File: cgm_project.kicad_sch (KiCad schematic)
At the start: 0 parts

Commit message: feat: complete power management block with tp4056 and ap2112k
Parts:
- added C1, C2, C3: 10uF, symbol Device:C_Small
- added D1: GREEN LED, symbol Device:LED
- added D2: RED LED, symbol Device:LED
- added J1: JST BATT CONNECTOR, symbol Connector_Generic:Conn_01x02
- added R1: 2k, symbol Device:R_Small
- added R2: 1k, symbol Device:R_Small
- added SW1: SW_SPDT, symbol Switch:SW_SPDT
- added U1: TP4056-42-ESOP8, Package_SO:SOIC-8-1EP_3.9x4.9mm_P1.27mm_EP2.41x3.3mm_ThermalVias, symbol Battery_Management:TP4056-42-ESOP8
- added U2: AP2112K-3.3, Package_TO_SOT_SMD:SOT-23-5, symbol Regulator_Linear:AP2112K-3.3
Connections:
- new net: D1.1 (K), U1.6 (~{STDBY})
- new net: D1.2 (A), D2.2 (A), R1.2
- new net: R2.1, U1.2 (PROG)
- new net: SW1.2 (B), U2.1 (VIN), U2.3 (EN)
- new net: D2.1 (K), U1.7 (~{CHRG})
- new net +3V3: C3.1, U2.5 (VOUT)
- new net GND: C1.1, C2.2, C3.2, J1.2 (Pin_2), R2.2, U1.1 (TEMP), U1.3 (GND), U2.2 (GND)
- new net VBAT: C2.1, J1.1 (Pin_1), SW1.1 (A), U1.5 (BAT)
- new net VBUS_5V: C1.2, R1.1, U1.4 (V_{CC}), U1.8 (CE)
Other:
- note added: "POWER MANAGEMENT"

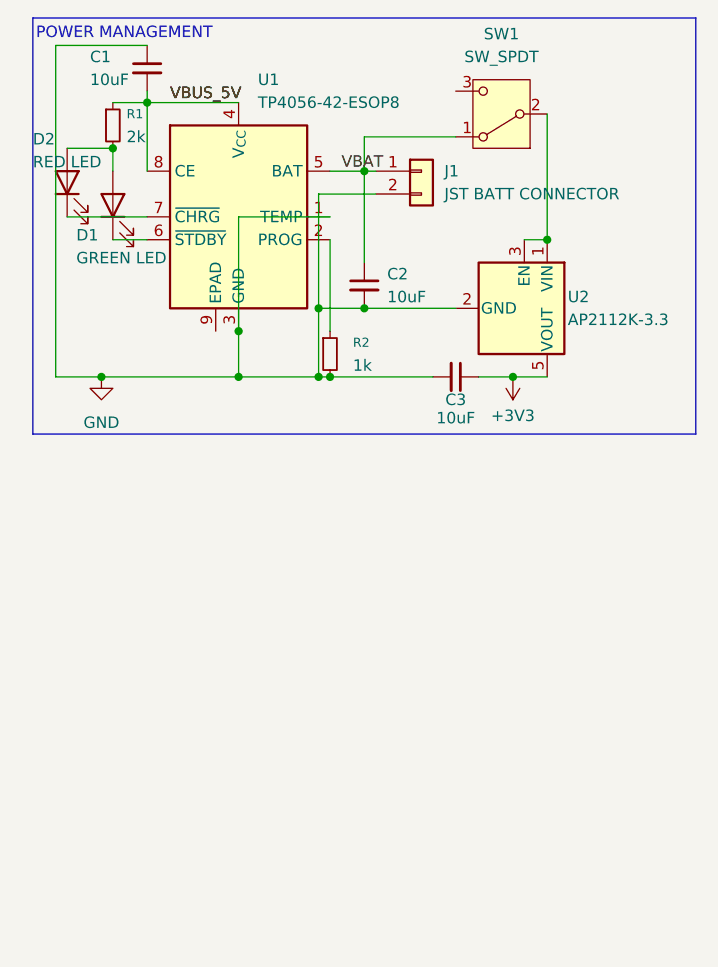
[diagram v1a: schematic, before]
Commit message: feat: implement fused native USB-C receptacle block
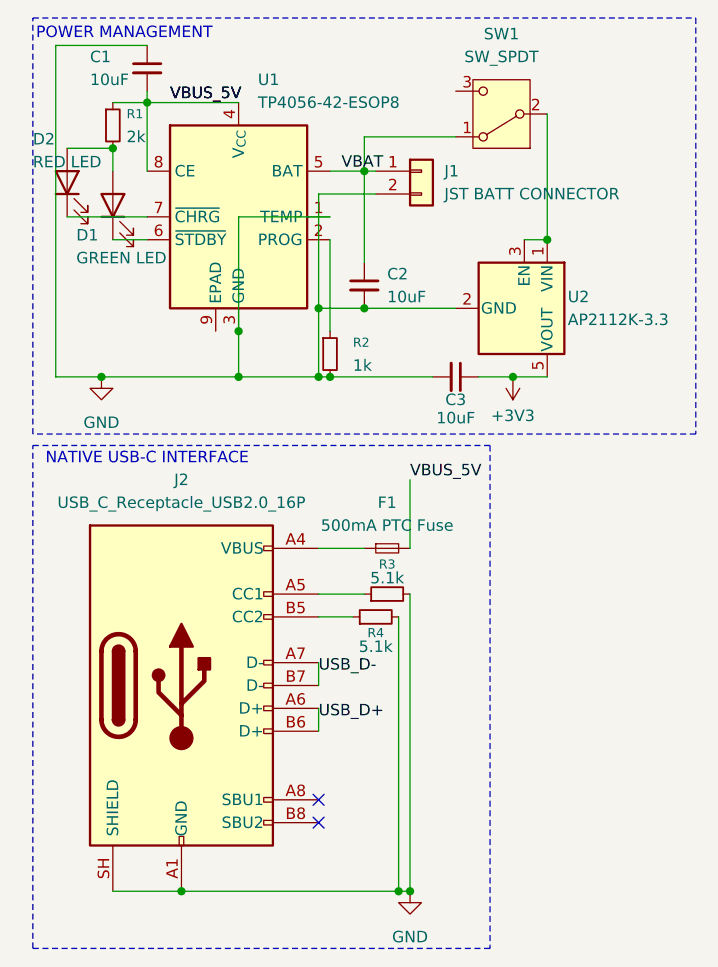
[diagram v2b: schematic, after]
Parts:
- added F1: 500mA PTC Fuse, symbol Device:Fuse_Small
- added J2: USB_C_Receptacle_USB2.0_16P, symbol Connector:USB_C_Receptacle_USB2.0_16P
- added R3, R4: 5.1k, symbol Device:R_Small
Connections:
- net GND: now also J2.A1 (GND), J2.A12 (GND), J2.B1 (GND), J2.B12 (GND), J2.SH (SHIELD), R3.2, R4.2
- net VBUS_5V: now also F1.2
- new net: J2.B5 (CC2), R4.1
- new net: F1.1, J2.A4 (VBUS), J2.A9 (VBUS), J2.B4 (VBUS), J2.B9 (VBUS)
- new net: J2.A5 (CC1), R3.1
- new net USB_D+: J2.A6 (D+), J2.B6 (D+)
- new net USB_D-: J2.A7 (D-), J2.B7 (D-)
- no-connect marks 0 -> 2
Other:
- note added: "NATIVE USB-C INTERFACE"

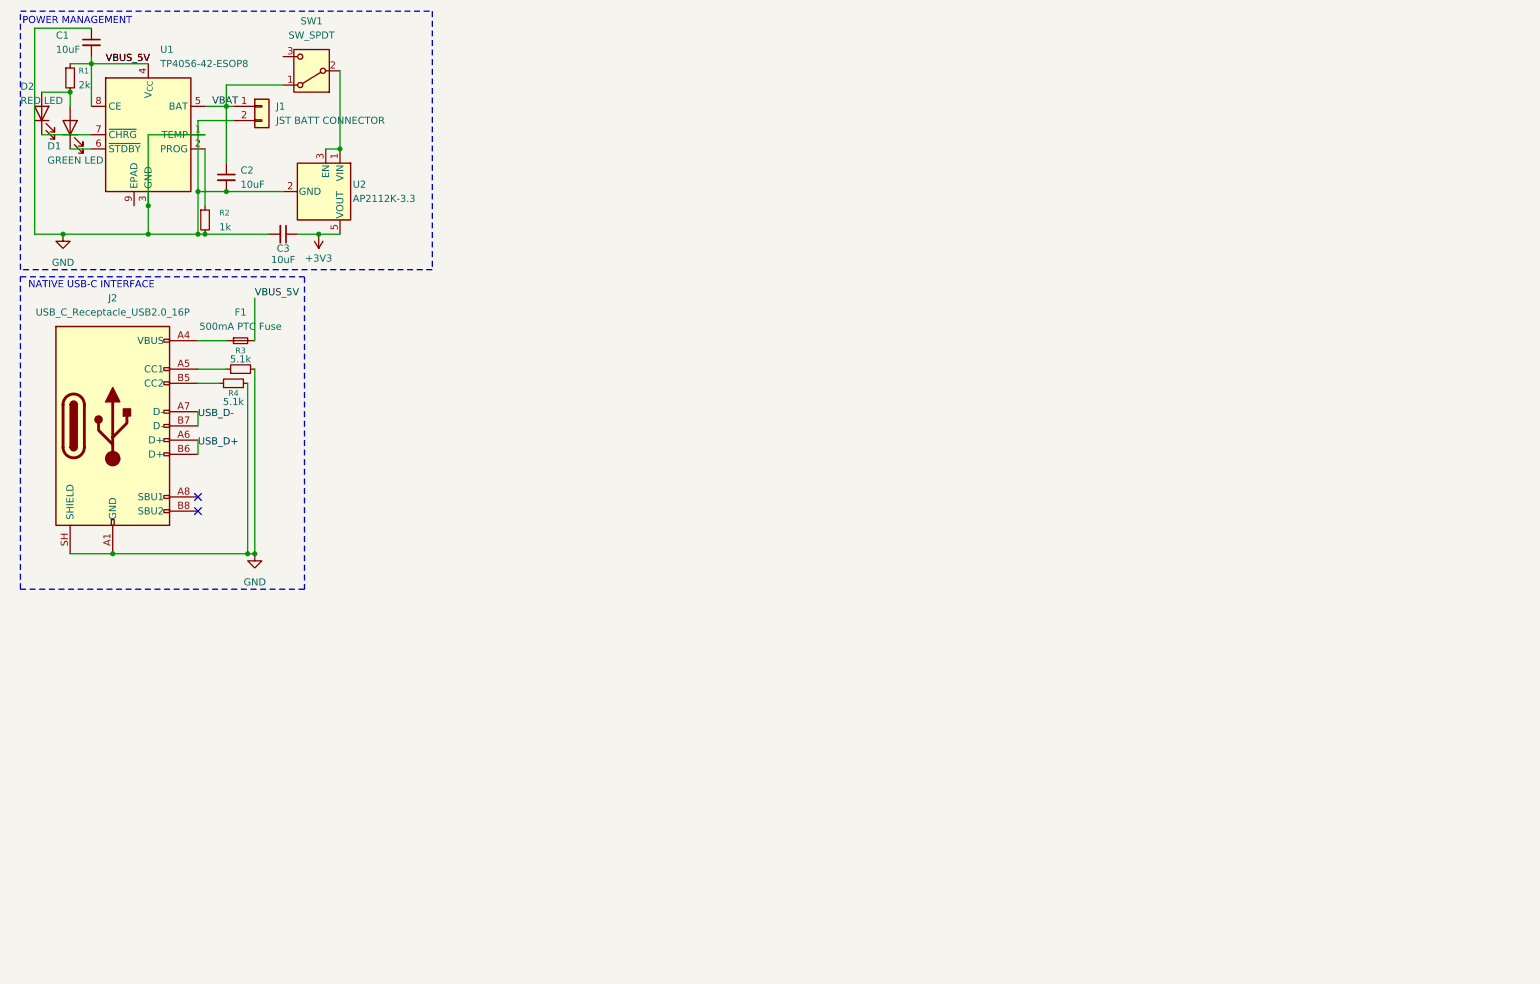
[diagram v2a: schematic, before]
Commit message: feat: implement esp32-c3 core with boot logic and net labels
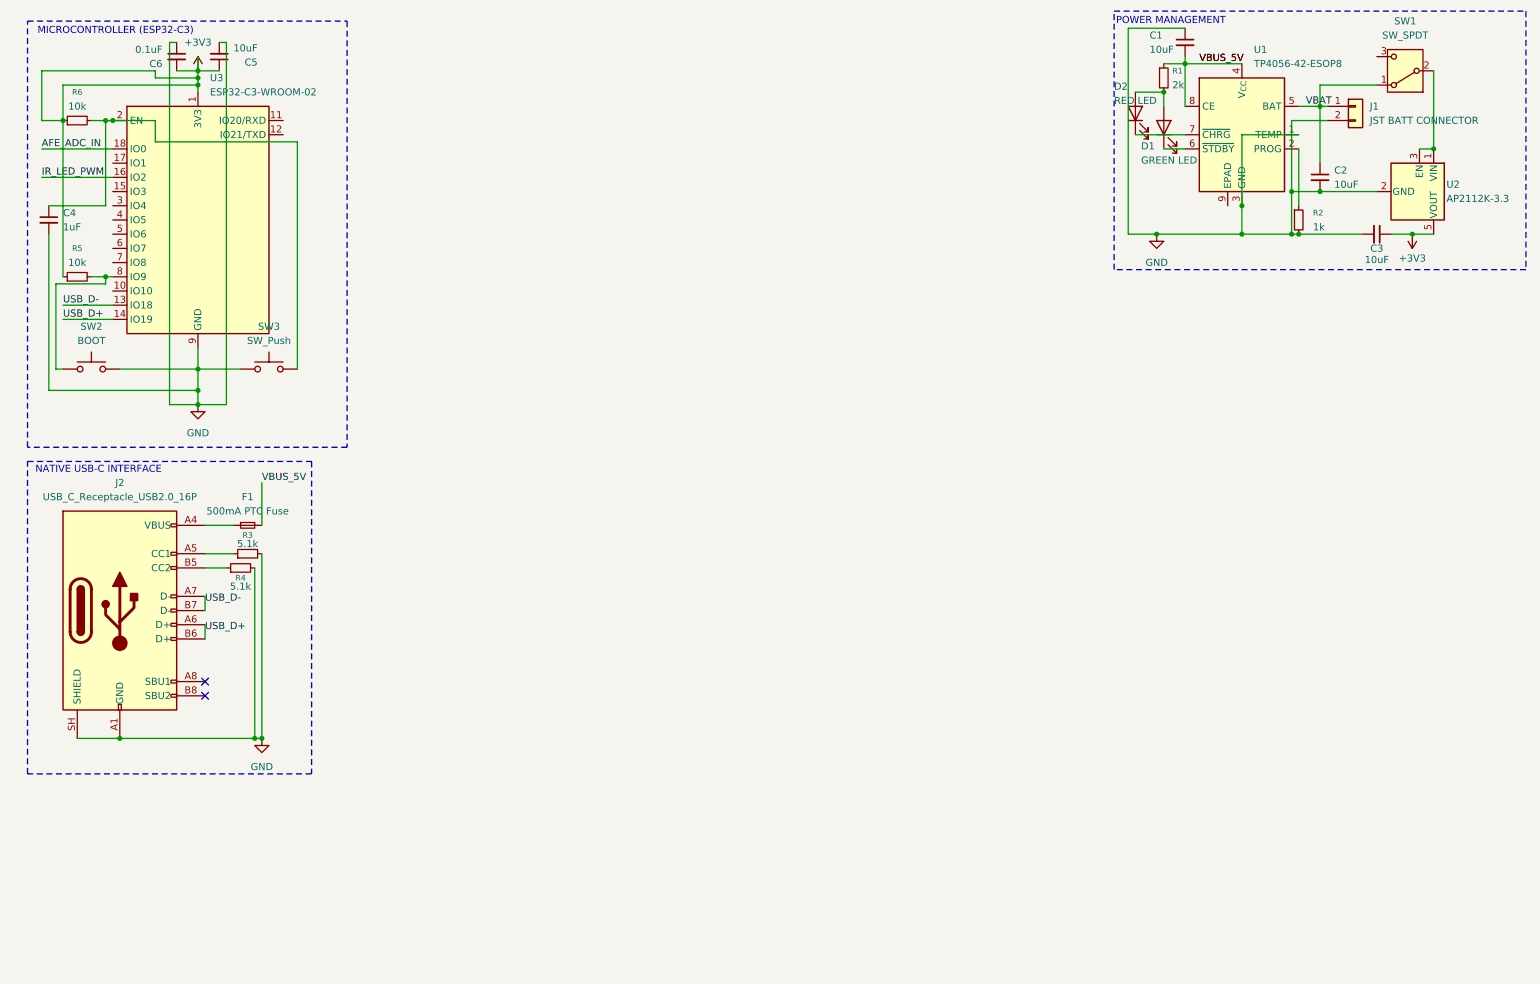
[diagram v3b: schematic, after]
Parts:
- added C4: 1uF, symbol Device:C_Small
- added C5: 10uF, symbol Device:C_Small
- added C6: 0.1uF, symbol Device:C_Small
- added R5, R6: 10k, symbol Device:R_Small
- added SW2: BOOT, symbol Switch:SW_Push
- added SW3: SW_Push, symbol Switch:SW_Push
- added U3: ESP32-C3-WROOM-02, RF_Module:ESP32-C3-WROOM-02, symbol RF_Module:ESP32-C3-WROOM-02
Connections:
- net +3V3: now also C5.1, C6.2, R5.1, R6.1, U3.1 (3V3)
- net GND: now also C4.2, C5.2, C6.1, SW2.2, SW3.1, U3.19 (GND), U3.9 (GND)
- net USB_D+: now also U3.14 (IO19)
- net USB_D-: now also U3.13 (IO18)
- new net: R5.2, SW2.1, U3.8 (IO9)
- new net: C4.1, R6.2, SW3.2, U3.2 (EN)
- new net AFE_ADC_IN: U3.18 (IO0)
- new net IR_LED_PWM: U3.16 (IO2)
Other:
- note added: "MICROCONTROLLER (ESP32-C3)"
- moved on the sheet: C1, C2, C3, D1, D2, F1, J1, J2, R1, R2, R3, R4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

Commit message: feat: implement OPA380 transimpedance amplifier and photodiode array
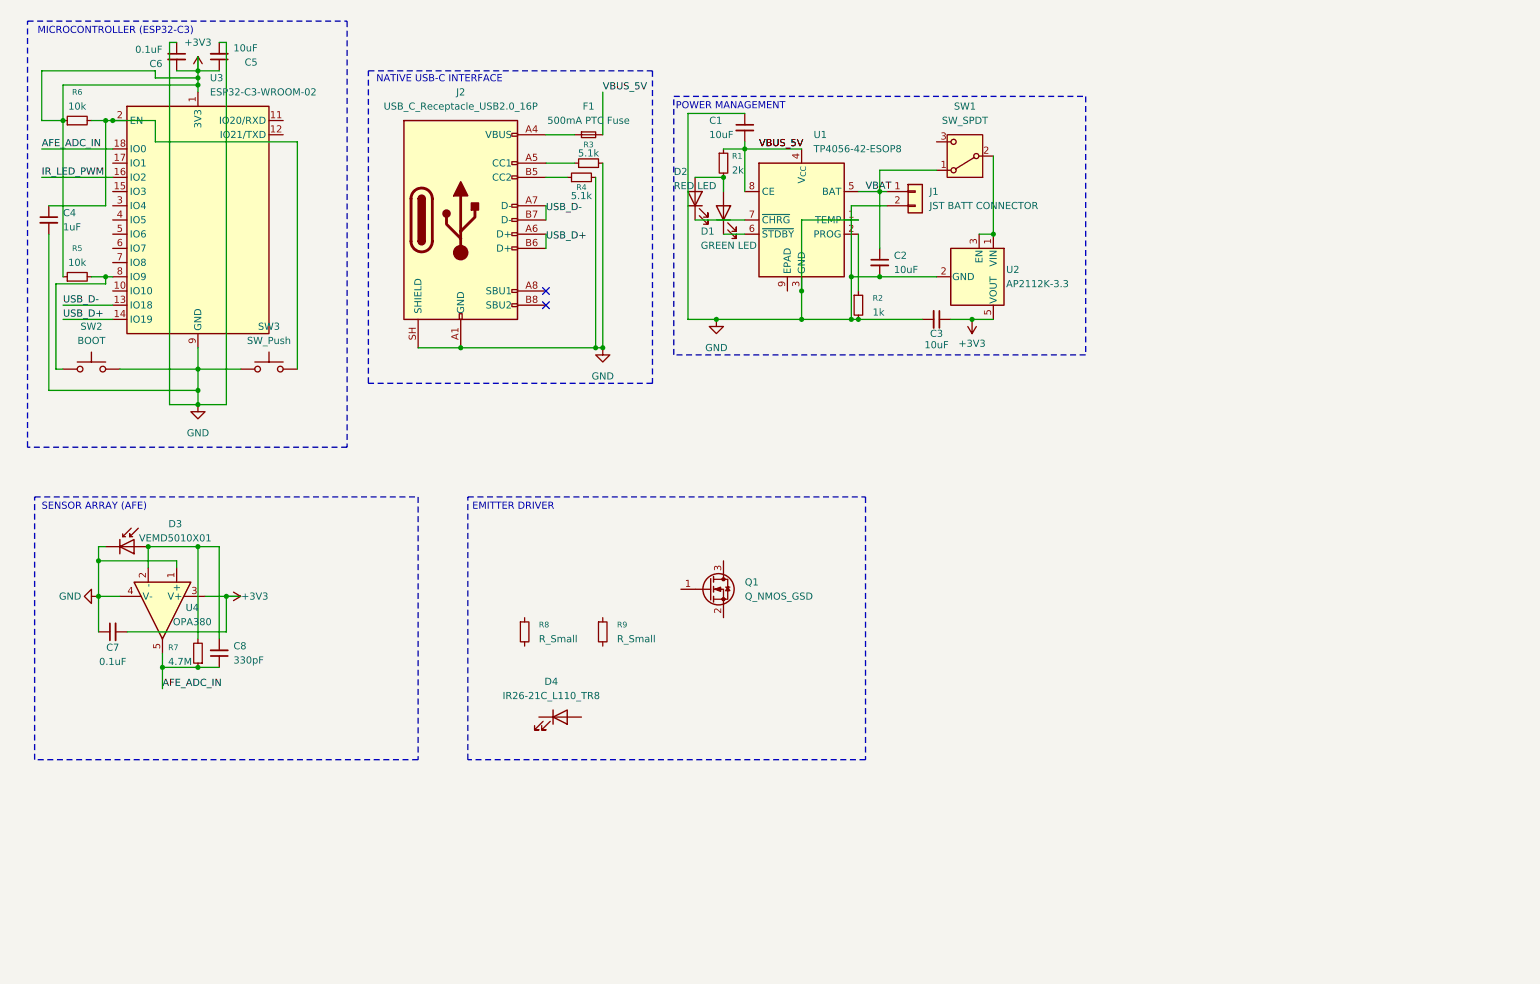
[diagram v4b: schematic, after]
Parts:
- added C7: 0.1uF, symbol Device:C_Small
- added C8: 330pF, symbol Device:C_Small
- added D3: VEMD5010X01, symbol Device:D_Photo
- added D4: IR26-21C_L110_TR8, LED_SMD:LED_1206_3216Metric, symbol LED:IR26-21C_L110_TR8
- added Q1: Q_NMOS_GSD, symbol Transistor_FET:Q_NMOS_GSD
- added R7: 4.7M, symbol Device:R_Small
- added R8, R9: R_Small, symbol Device:R_Small
- added U4: OPA380, symbol Simulation_SPICE:OPAMP
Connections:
- net +3V3: now also C7.2, U4.3 (V+)
- net AFE_ADC_IN: now also C8.1, R7.1, U4.5
- net GND: now also C7.1, D3.1 (K), U4.1 (+), U4.4 (V-)
- new net: C8.2, D3.2 (A), R7.2, U4.2 (-)
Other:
- note added: "EMITTER DRIVER"
- note added: "SENSOR ARRAY (AFE)"
- moved on the sheet: C1, C2, C3, D1, D2, F1, J1, J2, R1, R2, R3, R4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

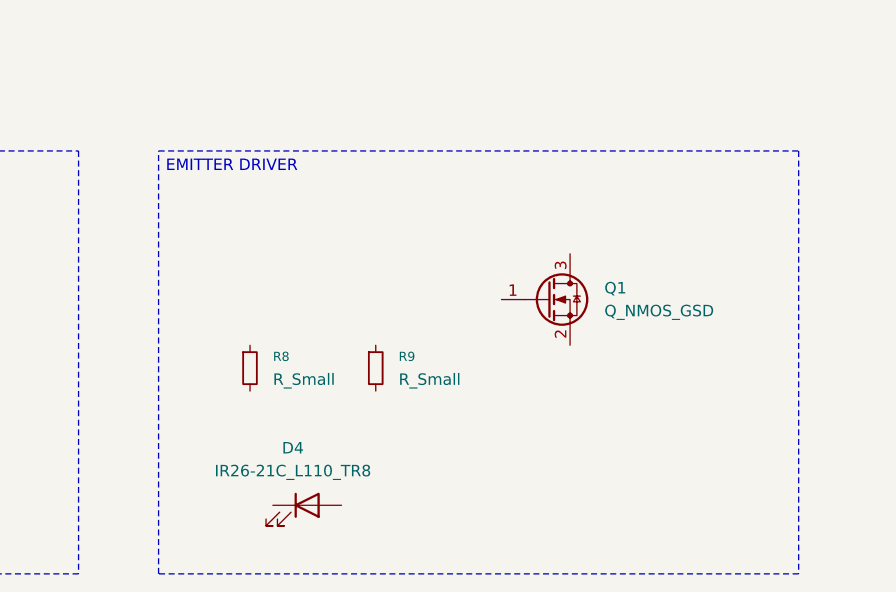
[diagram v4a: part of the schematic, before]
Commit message: feat: implement N-channel MOSFET emitter driver block
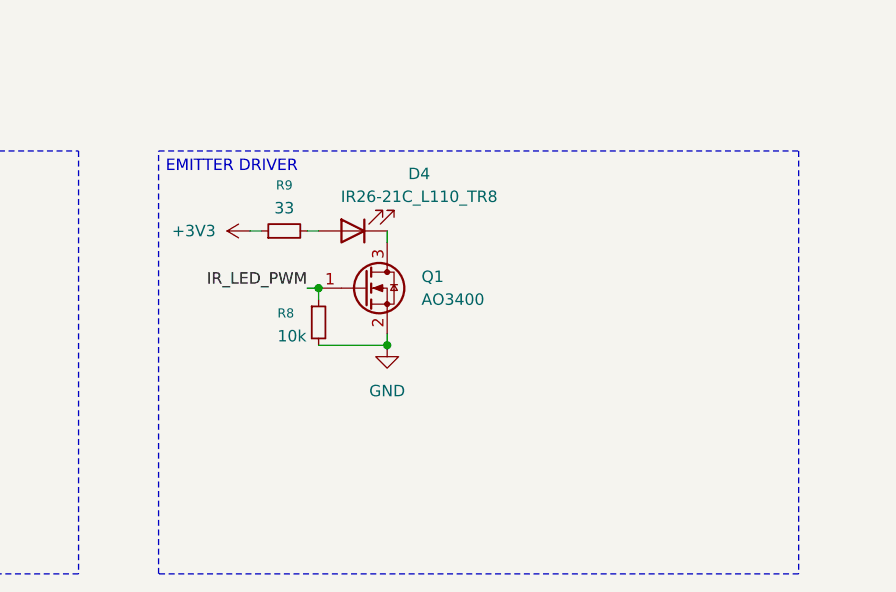
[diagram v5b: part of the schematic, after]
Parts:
- Q1: value Q_NMOS_GSD -> AO3400
- R8: value R_Small -> 10k
- R9: value R_Small -> 33
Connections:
- net +3V3: now also R9.1
- net GND: now also Q1.2 (S), R8.2
- net IR_LED_PWM: now also Q1.1 (G), R8.1
- net at D4.1 (K): now also Q1.3 (D)
- net at D4.2 (A): now also R9.2
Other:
- moved on the sheet: D4, Q1, R8, R9
